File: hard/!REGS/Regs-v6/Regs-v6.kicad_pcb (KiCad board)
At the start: 2 copper layers, 160 x 99.1 mm, 51 parts, among them J1 Conn_01x15_Female, J11 Conn_01x03_Male, J12 Conn_01x01_Male, J13 Conn_01x01_Male, J14 Conn_01x01_Male, J15 Conn_01x01_Male, J16 Screw_Terminal_01x02, J17 Conn_01x09_Male, J18 Conn_01x09_Male, J19 Conn_01x01_Male, J2 Conn_01x09_Male, J20 Conn_01x01_Male, J3 Conn_01x09_Male, J4 Conn_01x09_Male, J5 Conn_01x09_Male, J6 Conn_01x09_Male, J7 Conn_01x09_Male, J8 Conn_01x09_Male, Q1 IRLML5203, U1 REG_CNT, U10 REG_CNT, U11 REG_CNT, U12 REG_CNT, U13 74LS139, U14 74HC00, U15 MUX2-1, U16 REG_CNT, U17 REG_CNT, U18 REG_CNT, U19 REG_CNT, U2 REG_CNT, U3 REG_CNT, U4 REG_CNT, U5 REG_CNT, U6 REG_CNT, U7 REG_CNT, U8 REG_CNT, U9 REG_CNT

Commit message: Regs v6 in work
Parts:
- J2, J3, J4, J5, J6, J7, J8: value Conn_01x09_Male -> Conn_01x15_Female; footprint Connector_PinHeader_2.54mm:PinHeader_1x09_P2.54mm_Vertical -> Connector_PinSocket_2.54mm:PinSocket_1x15_P2.54mm_Vertical
- moved J8 203.7 mm to (204.9, 96.5)
- moved J7 169.4 mm to (200.3, 96.5)
- moved J6 147.7 mm to (195.7, 96.5)
- moved J5 126.3 mm to (191.1, 96.5)
- moved J3 5.24 mm to (105.4, 62.2)
- moved J4 5.24 mm to (87.6, 62.2)
- moved J2 5.24 mm to (123.2, 62.2)
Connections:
- J2 pad 1: GND -> /R1.0
- J2 pad 2: /R1.0 -> Net-(J2-Pad2)
- J2 pad 4: /R1.2 -> Net-(J2-Pad4)
- J2 pad 5: /R1.3 -> /R1.2
- J2 pad 6: /R1.4 -> Net-(J2-Pad6)
- J2 pad 7: /R1.5 -> /R1.3
- J2 pad 8: /R1.6 -> Net-(J2-Pad8)
- J2 pad 9: /R1.7 -> /R1.4
- J3 pad 1: GND -> /R2.0
- J3 pad 2: /R2.0 -> Net-(J3-Pad2)
- J3 pad 4: /R2.2 -> Net-(J3-Pad4)
- J3 pad 5: /R2.3 -> /R2.2
- J3 pad 6: /R2.4 -> Net-(J3-Pad6)
- J3 pad 7: /R2.5 -> /R2.3
- J3 pad 8: /R2.6 -> Net-(J3-Pad8)
- J3 pad 9: /R2.7 -> /R2.4
- J4 pad 1: GND -> /R3.0
- J4 pad 2: /R3.0 -> Net-(J4-Pad2)
- J4 pad 4: /R3.2 -> Net-(J4-Pad4)
- J4 pad 5: /R3.3 -> /R3.2
- J4 pad 6: /R3.4 -> Net-(J4-Pad6)
- J4 pad 7: /R3.5 -> /R3.3
- J4 pad 8: /R3.6 -> Net-(J4-Pad8)
- J4 pad 9: /R3.7 -> /R3.4
- J5 pad 1: GND -> /R4.0
- J5 pad 2: /R4.0 -> Net-(J5-Pad2)
- J5 pad 4: /R4.2 -> Net-(J5-Pad4)
- J5 pad 5: /R4.3 -> /R4.2
- J5 pad 6: /R4.4 -> Net-(J5-Pad6)
- J5 pad 7: /R4.5 -> /R4.3
- J5 pad 8: /R4.6 -> Net-(J5-Pad8)
- J5 pad 9: /R4.7 -> /R4.4
- J6 pad 1: GND -> /R5.0
- J6 pad 2: /R5.0 -> Net-(J6-Pad2)
- J6 pad 4: /R5.2 -> Net-(J6-Pad4)
- J6 pad 5: /R5.3 -> /R5.2
- J6 pad 6: /R5.4 -> Net-(J6-Pad6)
- J6 pad 7: /R5.5 -> /R5.3
- J6 pad 8: /R5.6 -> Net-(J6-Pad8)
- J6 pad 9: /R5.7 -> /R5.4
- J7 pad 1: GND -> /R6.0
- J7 pad 2: /R6.0 -> Net-(J7-Pad2)
- J7 pad 4: /R6.2 -> Net-(J7-Pad4)
- J7 pad 5: /R6.3 -> /R6.2
- J7 pad 6: /R6.4 -> Net-(J7-Pad6)
- J7 pad 7: /R6.5 -> /R6.3
- J7 pad 8: /R6.6 -> Net-(J7-Pad8)
- J7 pad 9: /R6.7 -> /R6.4
- J8 pad 1: GND -> /R7.0
- J8 pad 2: /R7.0 -> Net-(J8-Pad2)
- J8 pad 4: /R7.2 -> Net-(J8-Pad4)
- J8 pad 5: /R7.3 -> /R7.2
- J8 pad 6: /R7.4 -> Net-(J8-Pad6)
- J8 pad 7: /R7.5 -> /R7.3
- J8 pad 8: /R7.6 -> Net-(J8-Pad8)
- J8 pad 9: /R7.7 -> /R7.4
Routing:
- net GND: track 252.2 -> 198.8 mm
- net VCC: track 168.3 -> 114.9 mm
- net /R3.7: track 10.2 -> 13.5 mm
- net /R2.7: track 10.2 -> 13.5 mm
- net /R1.7: track 10.2 -> 13.5 mm
- net /R2.3: track 10.2 -> 8.25 mm
- net /R1.3: track 10.2 -> 8.26 mm
- net /R3.3: track 10.2 -> 8.26 mm
- net /R3.2: track 10.2 -> 8.67 mm
- net /R2.2: track 10.2 -> 8.67 mm
- net /R1.2: track 10.2 -> 8.67 mm
- net /R3.4: track 10.2 -> 8.67 mm
- net /R2.4: track 10.2 -> 8.67 mm
- net /R1.4: track 10.2 -> 8.67 mm
- net /~H: track 114.9 -> 116.0 mm
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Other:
- board text added: "01.06.25"
- board text removed: "22.05.25"

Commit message: Regs v6 in work
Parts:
- moved J8 191.5 mm to (16.5, 62.2)
- moved J7 169.5 mm to (34.3, 62.2)
- moved J6 147.7 mm to (52.1, 62.2)
- moved J5 126.0 mm to (69.8, 62.2)
- moved J12 15.3 mm to (84.5, 109.2)
- moved C1 6.35 mm to (43.2, 61.0)
- moved Q1 4.02 mm to (30.5, 101.6), turned to 0 degrees
- moved C3 0.64 mm to (77.5, 103.5)
- moved J17 0.63 mm to (170.8, 82.5)
- moved J18 0.63 mm to (170.8, 57.1)
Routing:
- net GND: track 198.8 -> 381.9 mm
- net VCC: track 114.9 -> 278.1 mm
- net /~R0: track 22.9 -> 157.1 mm, vias 0 -> 2
- net /~R1: track 22.9 -> 130.1 mm, vias 0 -> 1
- net /~R3: track 22.9 -> 109.9 mm, vias 0 -> 1
- net /~R2: track 22.9 -> 98.6 mm, vias 0 -> 1
- net /DST[0]: track 0.00 -> 22.9 mm
- net /R7.7: track 0.00 -> 19.4 mm
- net /R7.6: track 0.00 -> 17.2 mm
- net /R7.0: track 0.00 -> 17.2 mm
- net /R7.5: track 0.00 -> 15.4 mm
- net /R7.1: track 0.00 -> 15.4 mm
- net /R7.4: track 0.00 -> 12.5 mm
- net /R7.2: track 0.00 -> 12.5 mm
- net /R7.3: track 0.00 -> 11.4 mm
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
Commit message: Regs v6 in work
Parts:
- moved J19 115.3 mm to (33.0, 67.3)
- moved J20 100.9 mm to (51.4, 67.3)
- moved J13 45.4 mm to (86.4, 67.3)
- moved J11 30.7 mm to (49.5, 109.9), turned to 90 degrees
- moved U13 28.3 mm to (49.5, 106.7), turned to 90 degrees
- moved C3 28.0 mm to (49.5, 101.9), turned to 270 degrees
- moved J14 1.42 mm to (124.5, 102.2)
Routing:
- net /~Bank0: track 53.0 -> 264.5 mm, vias 0 -> 14
- net /~L: track 115.9 -> 237.5 mm, vias 0 -> 2
- net /~H: track 116.0 -> 224.3 mm, vias 0 -> 2
- net /~Bank1: track 131.8 -> 215.0 mm, vias 0 -> 2
- net /DST[0]: track 22.9 -> 0.00 mm
- net GND: track 381.9 -> 373.9 mm
- net /~R0: track 157.1 -> 152.8 mm, vias 2 -> 1
- net /~R2: track 98.6 -> 94.6 mm
- net /~R1: track 130.1 -> 126.1 mm
- net /~Res: track 135.9 -> 132.7 mm
- net /~R3: track 109.9 -> 107.4 mm
- net VCC: track 278.1 -> 276.2 mm
- net /Latch: track 10.2 -> 11.3 mm
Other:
- board text added: "ADD ACTIVE BANK LEDS!!!"
- board text added: "DST[0:2]"
- board text removed: "DST[2:0]"

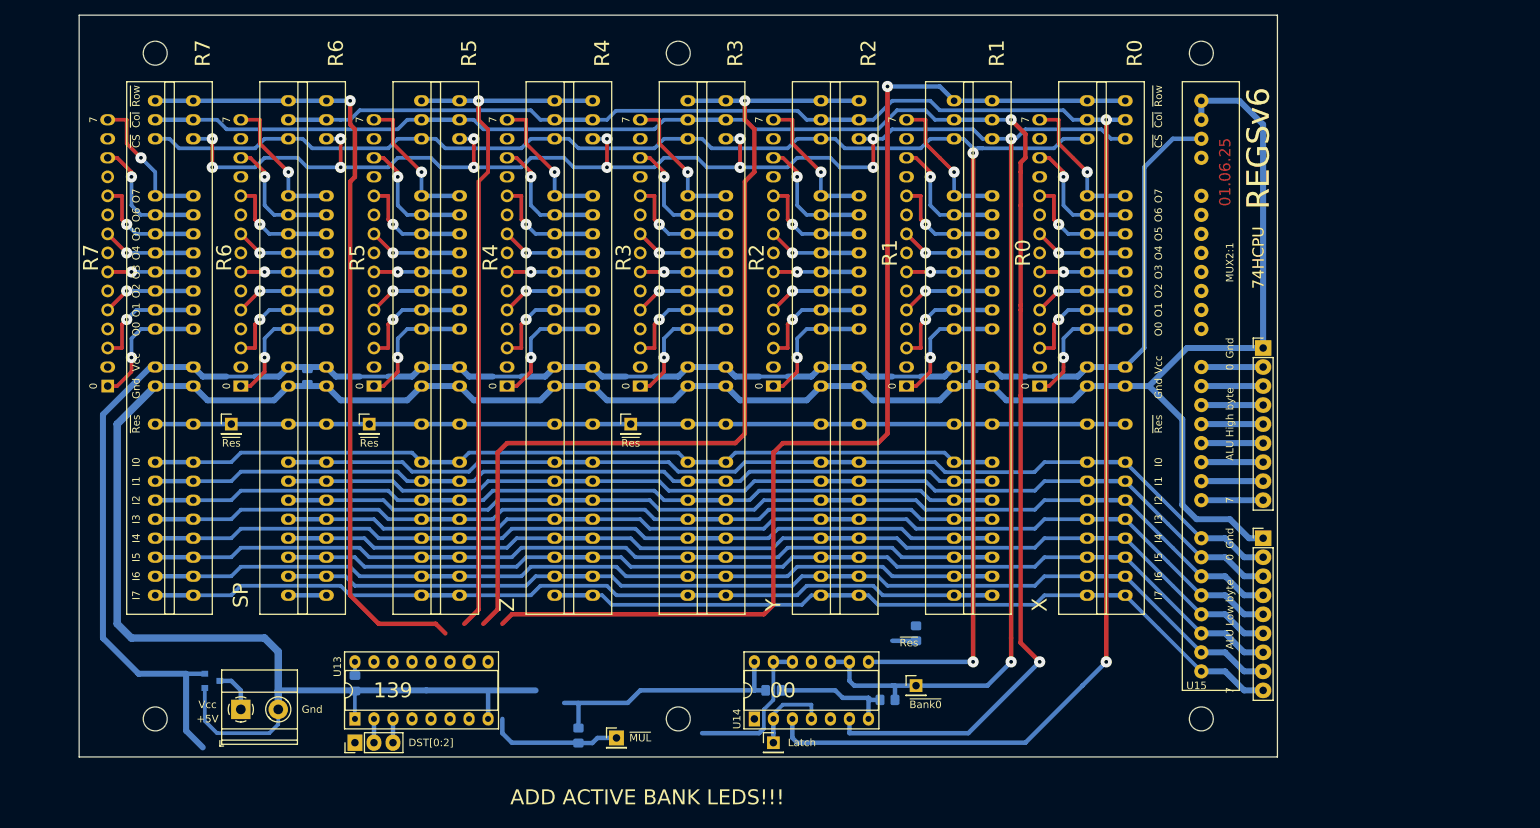
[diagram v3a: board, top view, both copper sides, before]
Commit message: Regs v6 pcb is almost ready
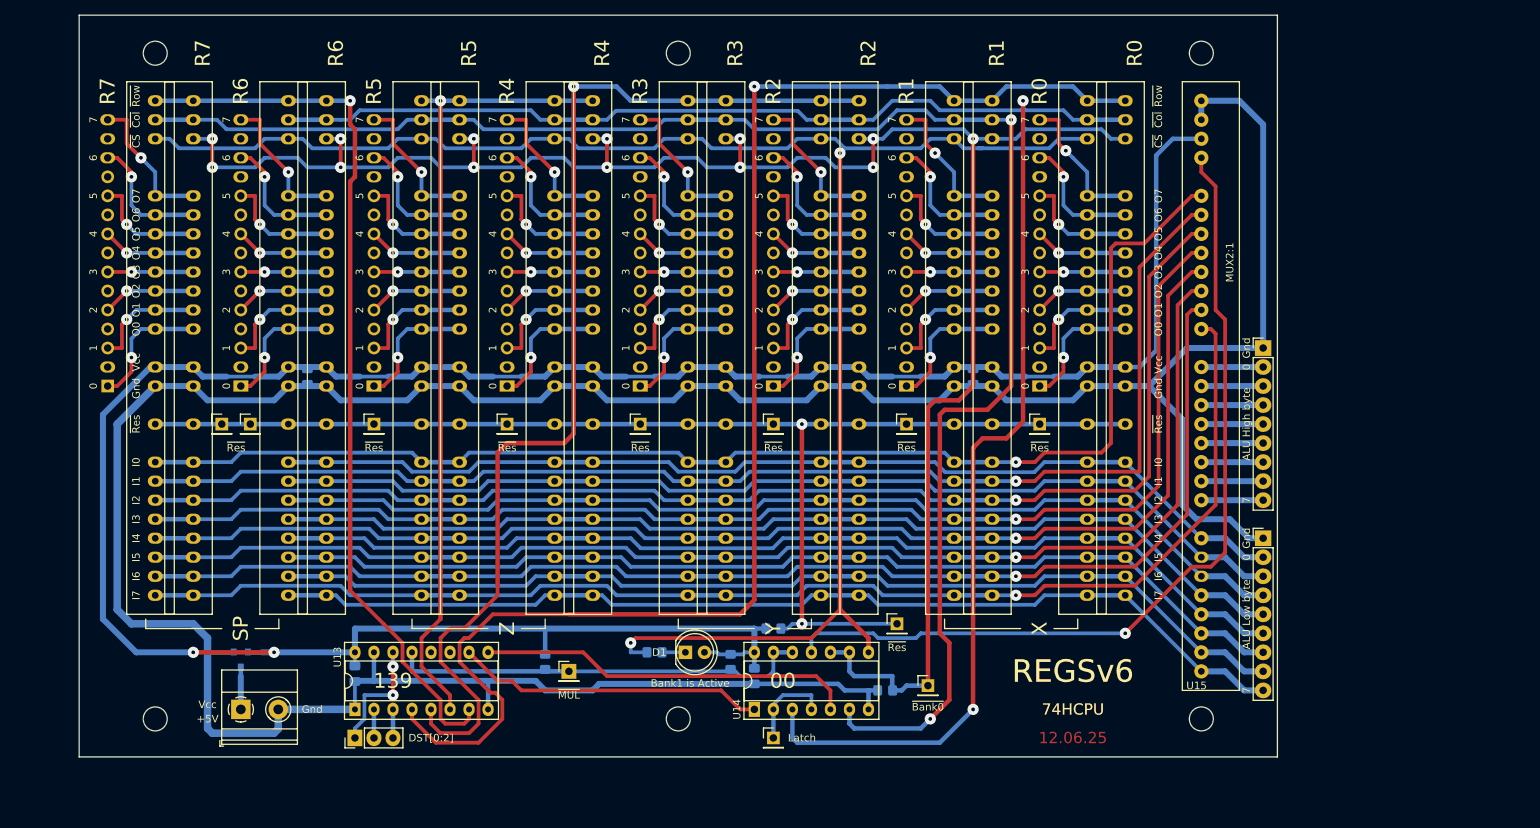
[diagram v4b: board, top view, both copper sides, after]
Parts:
- added D1: LED, LED_THT:LED_D5.0mm, F.Cu at (93.7, 97.8)
- added J10: Conn_01x01_Male, Connector_PinHeader_2.54mm:PinHeader_1x01_P2.54mm_Vertical, F.Cu at (141.0, 67.3)
- added J21: Conn_01x01_Male, Connector_PinHeader_2.54mm:PinHeader_1x01_P2.54mm_Vertical, F.Cu at (105.4, 67.3)
- added J22: Conn_01x01_Male, Connector_PinHeader_2.54mm:PinHeader_1x01_P2.54mm_Vertical, F.Cu at (31.8, 67.3)
- added J23: Conn_01x01_Male, Connector_PinHeader_2.54mm:PinHeader_1x01_P2.54mm_Vertical, F.Cu at (123.2, 67.3)
- added J24: Conn_01x01_Male, Connector_PinHeader_2.54mm:PinHeader_1x01_P2.54mm_Vertical, F.Cu at (69.8, 67.3)
- added J9: Conn_01x01_Male, Connector_PinHeader_2.54mm:PinHeader_1x01_P2.54mm_Vertical, F.Cu at (121.9, 94.0)
- added R1: 1k, Resistor_SMD:R_0805_2012Metric_Pad1.20x1.40mm_HandSolder, B.Cu at (89.5, 97.8)
- added R2: 10k, Resistor_SMD:R_0805_2012Metric_Pad1.20x1.40mm_HandSolder, B.Cu at (99.7, 99.1)
- moved R6 19.1 mm to (105.4, 94.6), turned to 180 degrees
- moved J12 10.9 mm to (78.1, 100.3)
- moved R5 10.8 mm to (74.9, 99.1)
- moved Q1 4.76 mm to (34.3, 98.7), turned to 270 degrees
- moved C4 3.17 mm to (102.9, 101.0), turned to 270 degrees
- moved J19 2.54 mm to (35.6, 67.3)
- moved J14 1.59 mm to (126.0, 102.2)
- moved R7 1.31 mm to (120.3, 102.9)
- moved C3 1.27 mm to (49.5, 100.6)
- moved U13 1.27 mm to (49.5, 105.4)
- moved U14 1.27 mm to (102.9, 105.4)
- moved J13 1.27 mm to (87.6, 67.3)
- moved J11 0.64 mm to (49.5, 109.2)
- moved J15 0.64 mm to (105.4, 109.2)
- moved J20 0.63 mm to (52.1, 67.3)
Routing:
- net Net-(U14-Pad11): track 0.00 -> 116.4 mm, vias 0 -> 1
- net /H7: track 114.9 -> 174.8 mm, vias 0 -> 1
- net /H1: track 114.9 -> 173.6 mm, vias 0 -> 1
- net /H5: track 114.9 -> 173.2 mm, vias 0 -> 1
- net /H3: track 114.9 -> 173.2 mm, vias 0 -> 1
- net /H6: track 114.9 -> 173.2 mm, vias 0 -> 1
- net /H4: track 114.9 -> 173.2 mm, vias 0 -> 1
- net /H2: track 114.9 -> 173.2 mm, vias 0 -> 1
- net /H0: track 114.9 -> 172.8 mm, vias 0 -> 1
- net Net-(U13-Pad9): track 0.00 -> 50.4 mm
- net VCC: track 276.2 -> 326.4 mm, vias 0 -> 2
- net Net-(U13-Pad10): track 0.00 -> 41.3 mm
- net /~Res: track 132.7 -> 172.0 mm, vias 0 -> 2
- net /~R0: track 152.8 -> 191.1 mm
- net /L7: track 107.1 -> 138.6 mm
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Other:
- board text added: "1"
- board text added: "12.06.25"
- board text added: "2"
- board text added: "3"
- board text added: "4"
- board text added: "5"
- board text added: "6"
- board text added: "Bank1 is Active"
- board text removed: "01.06.25"
- board text removed: "ADD ACTIVE BANK LEDS!!!"

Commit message: Regs v6 pcb is ready!
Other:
- board text added: "R0'"
- board text added: "R1'"
- board text added: "R2'"
- board text added: "R3'"
- board text added: "R4'"
- board text added: "R5'"
- board text added: "R6'"
- board text added: "R7'"

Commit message: Polishing Regs v6
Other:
- board text added: "13.08.25"
- board text removed: "12.06.25"
